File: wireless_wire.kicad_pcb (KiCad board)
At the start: 2 copper layers, 33 x 31.5 mm, 21 parts, among them SW1 SW_Push, SW2 SW_Push, U2 TLV75533PDBV, U3 ESP32-S3-WROOM-1, X1 USB4085-GF-A

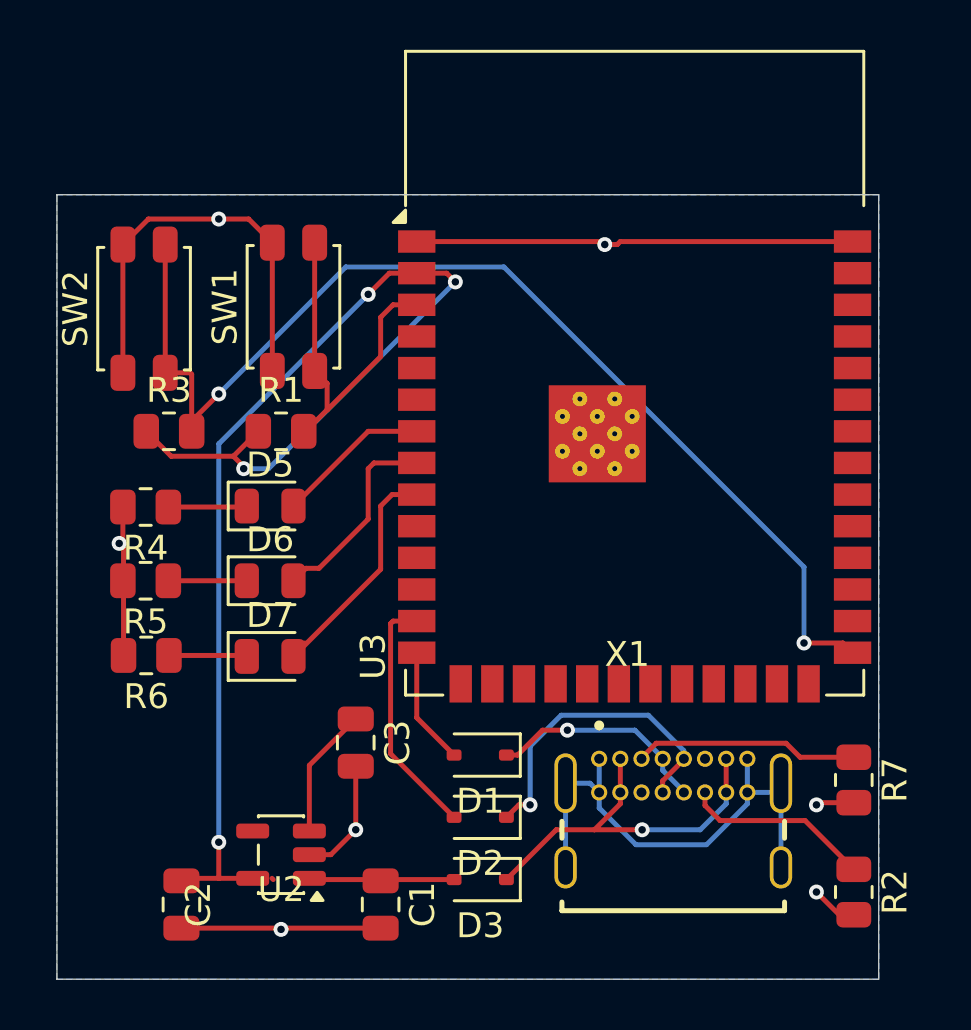
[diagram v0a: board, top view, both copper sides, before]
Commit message: fixed silkscreen and BOM finished
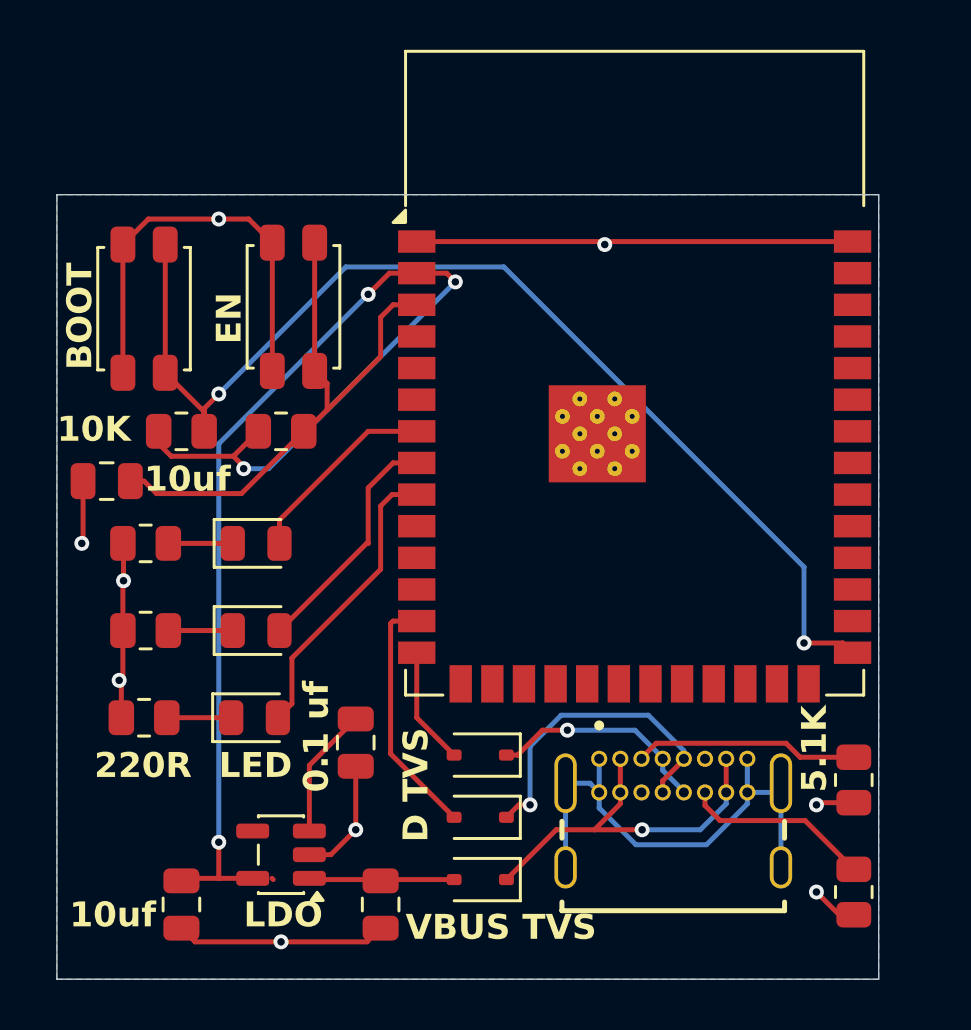
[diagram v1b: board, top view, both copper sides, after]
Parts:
- added C4: 10 uf, Capacitor_SMD:C_0805_2012Metric, F.Cu at (110.0, 84.5)
- D3: value D_TVS -> D_TVS_VBUS
- R1, R3: value R -> 10k
- R4, R5, R6: value R -> 220
- moved D7 2.54 mm to (115.9, 94.0)
- moved R6 2.50 mm to (111.5, 94.0)
- moved D6 2.08 mm to (116.0, 90.5)
- moved R5 2.00 mm to (111.6, 90.5)
- moved D5 1.60 mm to (116.0, 87.0)
- moved R4 1.46 mm to (111.6, 87.0)
- moved R3 0.50 mm to (113.0, 82.5)
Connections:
- D1 pad 2: /usb-u -> /usb-u_esp
- D2 pad 2: /usb-d -> /usb-d_esp
- U3 pad 13: /usb-d -> /usb-d_esp
- U3 pad 14: /usb-u -> /usb-u_esp
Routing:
- net /usb-d: track 22.7 -> 12.8 mm
- net /usb-d_esp: track 0.00 -> 9.93 mm
- net /EN: track 14.5 -> 22.7 mm
- net /usb-u_esp: track 0.00 -> 4.73 mm
- net /usb-u: track 13.6 -> 8.89 mm
- net GND: track 78.4 -> 82.3 mm, vias 7 -> 9
- net /LED3: track 9.89 -> 11.8 mm
- net /LED1: track 6.19 -> 7.93 mm
- net /LED2: track 8.10 -> 9.61 mm
- net /BOOT: track 46.2 -> 45.7 mm
- net Net-(D5-K): track 3.17 -> 2.59 mm
- net Net-(D6-K): track 3.15 -> 2.59 mm
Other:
- board text added: "0.1 uf"
- board text added: "10K"
- board text added: "10uf"
- board text added: "220R"
- board text added: "5.1K"
- board text added: "BOOT"
- board text added: "D TVS"
- board text added: "EN"
- board text added: "LDO"
- board text added: "LED"
- board text added: "VBUS TVS"
